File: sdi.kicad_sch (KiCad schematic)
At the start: 74 parts, among them J2 031-70526-21, J3 031-70526-21, U11 LIFCL-40-9BG256C, U15 GS2971A, U16 GS2988, Y1 ABM7_27.000MH_D2Y_T

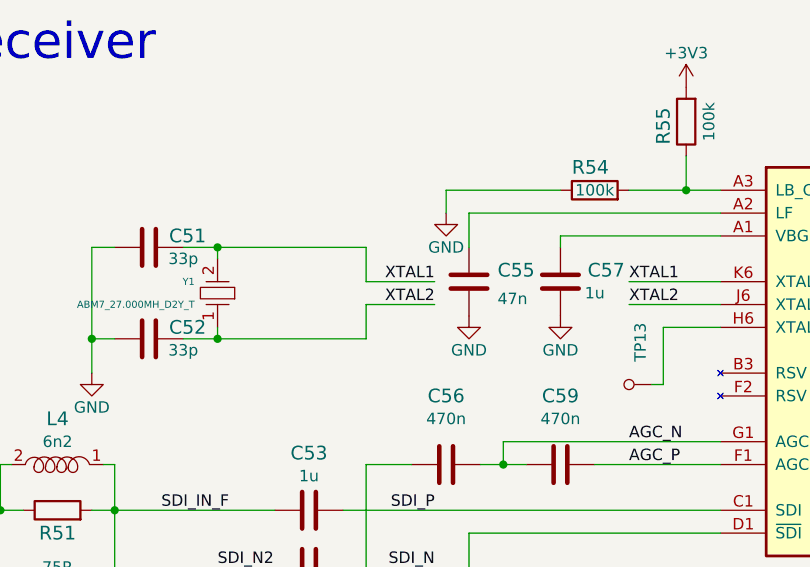
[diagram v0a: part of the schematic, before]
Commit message: Routed rest of low speed signals
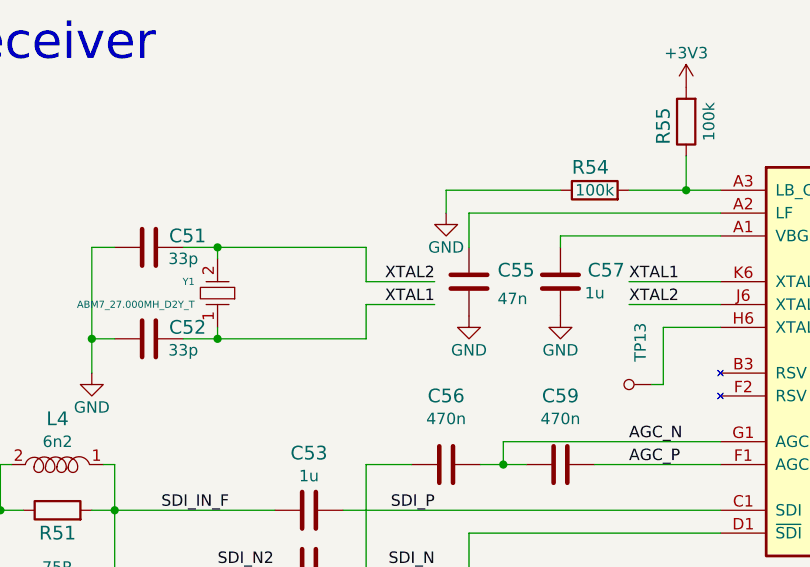
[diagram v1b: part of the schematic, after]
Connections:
- net XTAL1: now also C52.2, Y1.1; no longer C51.2, Y1.2
- net XTAL2: now also C51.2, Y1.2; no longer C52.2, Y1.1
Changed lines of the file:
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@@
     (effects (font (size 1.27 1.27)) (justify right bottom))
   )
-  (label "XTAL1" (at 78.74 177.8 180)
+  (label "XTAL1" (at 78.74 180.34 180)
     (effects (font (size 1.27 1.27)) (justify right bottom))
   )
@@
     (effects (font (size 1.27 1.27)) (justify right bottom))
   )
-  (label "XTAL2" (at 78.74 180.34 180)
+  (label "XTAL2" (at 78.74 177.8 180)
     (effects (font (size 1.27 1.27)) (justify right bottom))
   )

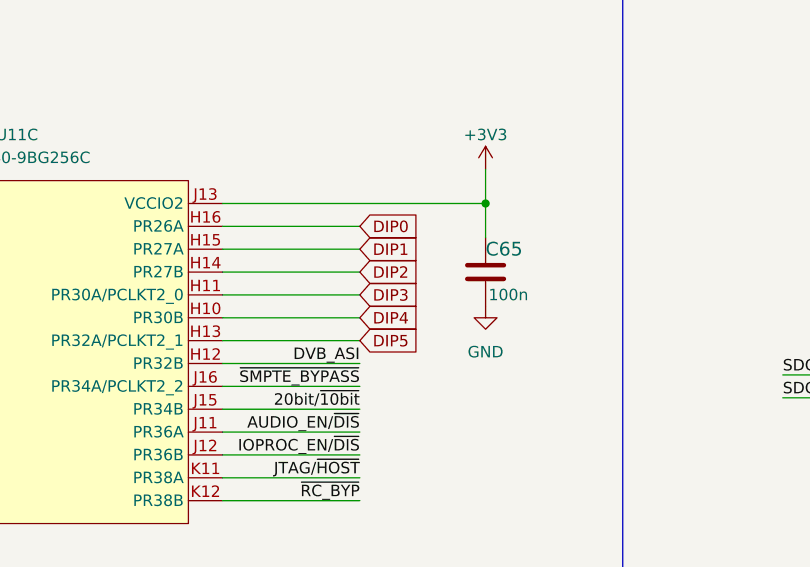
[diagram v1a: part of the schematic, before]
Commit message: Added gpio connector
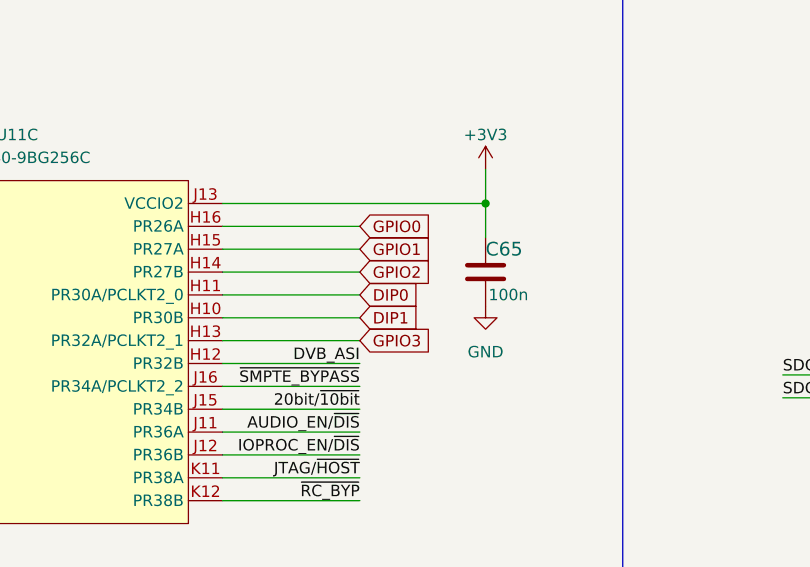
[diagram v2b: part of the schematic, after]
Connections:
- net DIP3 is gone; now on net DIP0: U11.H11 (PR30A/PCLKT2_0)
- net DIP4 is gone; now on net DIP1: U11.H10 (PR30B)
- net DIP0: no longer U11.H16 (PR26A)
- net DIP1: no longer U11.H15 (PR27A)
- net DIP2 renamed GPIO2
- net DIP5 renamed GPIO3
- new net GPIO0: U11.H16 (PR26A)
- new net GPIO1: U11.H15 (PR27A)
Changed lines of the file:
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@@
     )
   )
-  (global_label "DIP0" (shape input) (at 195.58 66.04 0) (fields_autoplaced)
+  (global_label "GPIO0" (shape input) (at 195.58 66.04 0) (fields_autoplaced)
     (effects (font (size 1.27 1.27)) (justify left))
-    (property "Intersheet References" "${INTERSHEET_REFS}" (id 0) (at 202.3474 65.9606 0)
+    (property "Intersheet References" "${INTERSHEET_REFS}" (id 0) (at 203.6779 65.9606 0)
       (effects (font (size 1.27 1.27)) (justify left) hide)
     )
   )
-  (global_label "DIP3" (shape input) (at 195.58 73.66 0) (fields_autoplaced)
+  (global_label "DIP0" (shape input) (at 195.58 73.66 0) (fields_autoplaced)
     (effects (font (size 1.27 1.27)) (justify left))
     (property "Intersheet References" "${INTERSHEET_REFS}" (id 0) (at 202.3474 73.5806 0)
@@
     )
   )
-  (global_label "DIP1" (shape input) (at 195.58 68.58 0) (fields_autoplaced)
+  (global_label "GPIO1" (shape input) (at 195.58 68.58 0) (fields_autoplaced)
     (effects (font (size 1.27 1.27)) (justify left))
-    (property "Intersheet References" "${INTERSHEET_REFS}" (id 0) (at 202.3474 68.5006 0)
+    (property "Intersheet References" "${INTERSHEET_REFS}" (id 0) (at 203.6779 68.5006 0)
       (effects (font (size 1.27 1.27)) (justify left) hide)
     )
@@
     )
   )
-  (global_label "DIP5" (shape input) (at 195.58 78.74 0) (fields_autoplaced)
+  (global_label "GPIO3" (shape input) (at 195.58 78.74 0) (fields_autoplaced)
     (effects (font (size 1.27 1.27)) (justify left))
-    (property "Intersheet References" "${INTERSHEET_REFS}" (id 0) (at 202.3474 78.6606 0)
+    (property "Intersheet References" "${INTERSHEET_REFS}" (id 0) (at 203.6779 78.6606 0)
       (effects (font (size 1.27 1.27)) (justify left) hide)
     )
@@
     )
   )
-  (global_label "DIP2" (shape input) (at 195.58 71.12 0) (fields_autoplaced)
+  (global_label "GPIO2" (shape input) (at 195.58 71.12 0) (fields_autoplaced)
     (effects (font (size 1.27 1.27)) (justify left))
-    (property "Intersheet References" "${INTERSHEET_REFS}" (id 0) (at 202.3474 71.0406 0)
+    (property "Intersheet References" "${INTERSHEET_REFS}" (id 0) (at 203.6779 71.0406 0)
       (effects (font (size 1.27 1.27)) (justify left) hide)
     )
   )
-  (global_label "DIP4" (shape input) (at 195.58 76.2 0) (fields_autoplaced)
+  (global_label "DIP1" (shape input) (at 195.58 76.2 0) (fields_autoplaced)
     (effects (font (size 1.27 1.27)) (justify left))
     (property "Intersheet References" "${INTERSHEET_REFS}" (id 0) (at 202.3474 76.1206 0)

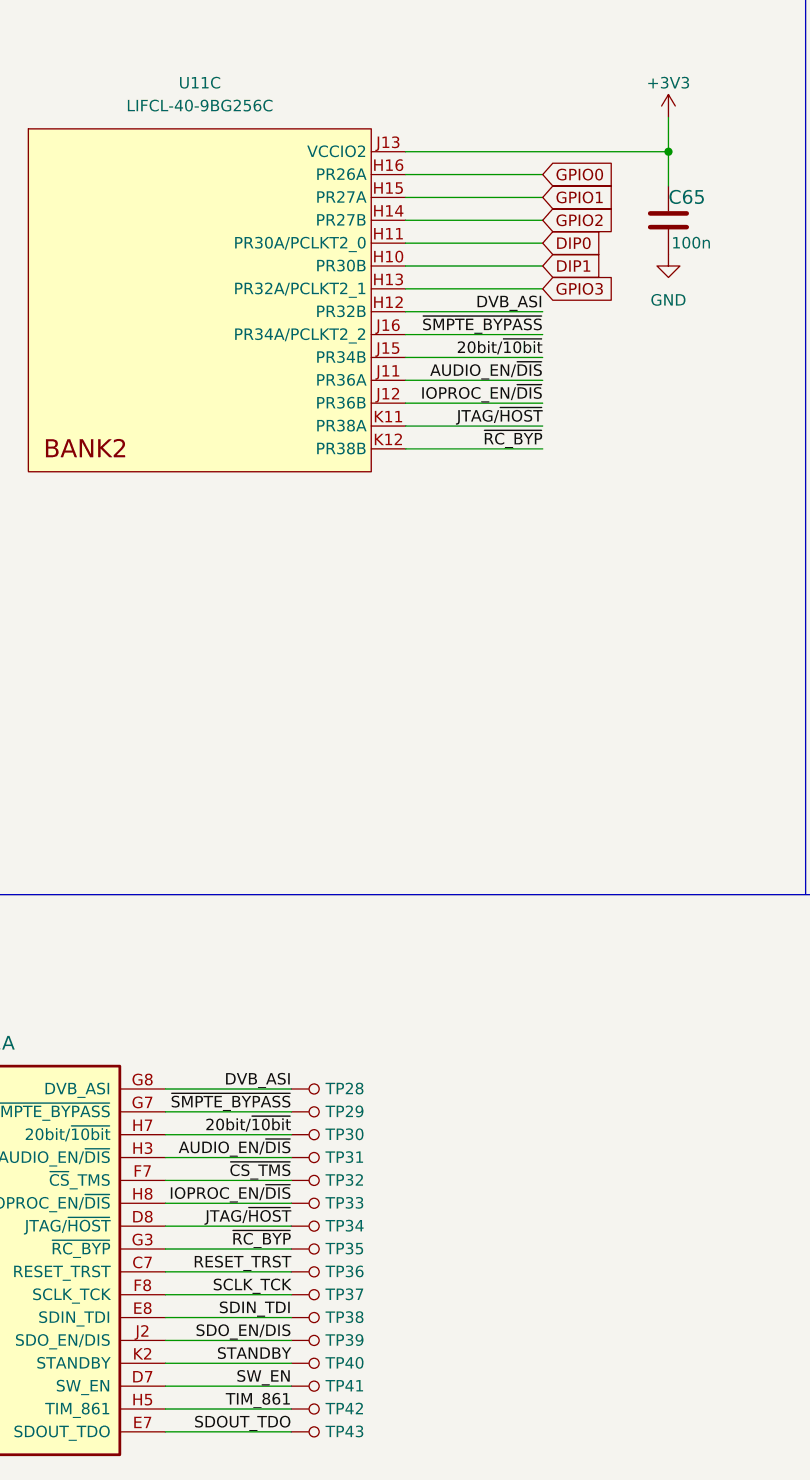
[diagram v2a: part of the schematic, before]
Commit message: Added FT230XQ-R for USB connectivity
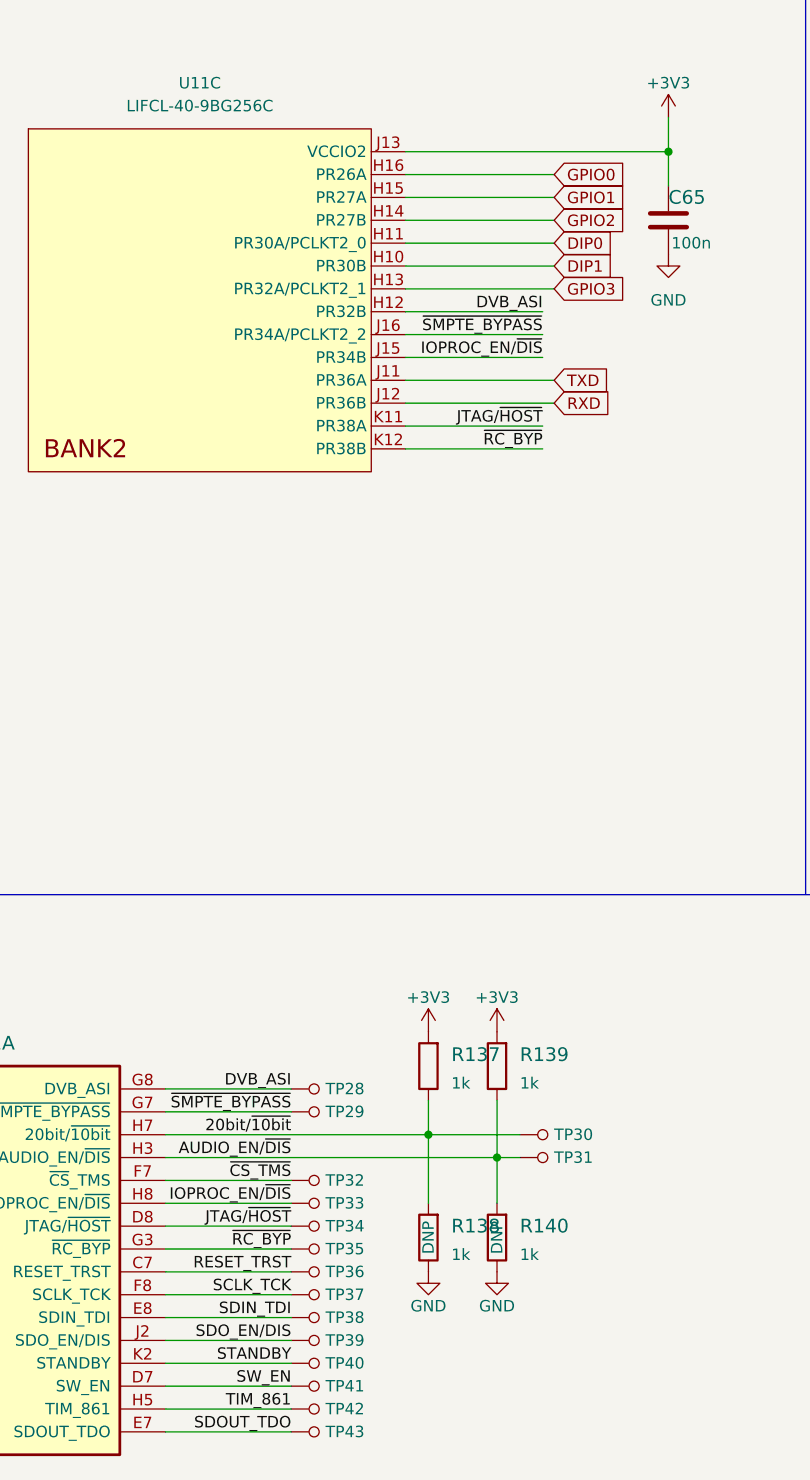
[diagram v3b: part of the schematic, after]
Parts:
- added R137, R138, R139, R140: R_1k_0402, antmicro-footprints:0402-res, symbol antmicroResistors0402:R_1k_0402
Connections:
- net +3V3: now also R137.2, R139.2
- net 20bit/~{10bit}: now also R137.1, R138.2; no longer U11.J15 (PR34B)
- net AUDIO_EN/~{DIS}: now also R139.1, R140.2; no longer U11.J11 (PR36A)
- net GND: now also R138.1, R140.1
- net IOPROC_EN/~{DIS}: now also U11.J15 (PR34B); no longer U11.J12 (PR36B)
- new net RXD: U11.J12 (PR36B)
- new net TXD: U11.J11 (PR36A)
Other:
- moved on the sheet: TP30, TP31

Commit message: Created loclib
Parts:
- R100, R101: footprint antmicro-footprints:0603-res -> crosslink-nx-video-converter-footprints:0603-res; symbol antmicroResistors0603:R_200R_0603 -> crosslink-nx-video-converter:R_200R_0603
- R137, R138, R139, R140: footprint antmicro-footprints:0402-res -> crosslink-nx-video-converter-footprints:0402-res; symbol antmicroResistors0402:R_1k_0402 -> crosslink-nx-video-converter:R_1k_0402
- U11: footprint antmicro-footprints:BGA-256_16x16_14.0x14.0mm -> crosslink-nx-video-converter-footprints:BGA-256_16x16_14.0x14.0mm; symbol antmicroBGAchips:LIFCL-40-9BG256C -> crosslink-nx-video-converter:LIFCL-40-9BG256C

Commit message: Added revision and title to the schematic sheets
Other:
- title: (none) -> CrossLink-NX Video Converter
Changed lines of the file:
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@@
 (kicad_sch (version 20211123) (generator eeschema)
   (paper "A3")
+  (title_block
+    (title "CrossLink-NX Video Converter")
+    (date "2022-10-27")
+    (rev "1.0.0")
+    (comment 1 "www.antmicro.com")
+    (comment 2 "Antmicro Ltd.")
+  )
   (junction (at 260.35 212.09) (diameter 0) (color 0 0 0 0)
   )
